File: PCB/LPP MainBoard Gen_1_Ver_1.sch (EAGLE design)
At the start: 48 parts, among them IC1 FE1.1S, U1 MAX15070, U3 IFX007T, U4 MAX15070, U5 IFX007T, U7 Pill STM32G431, U8 Blue Pill STM32F103

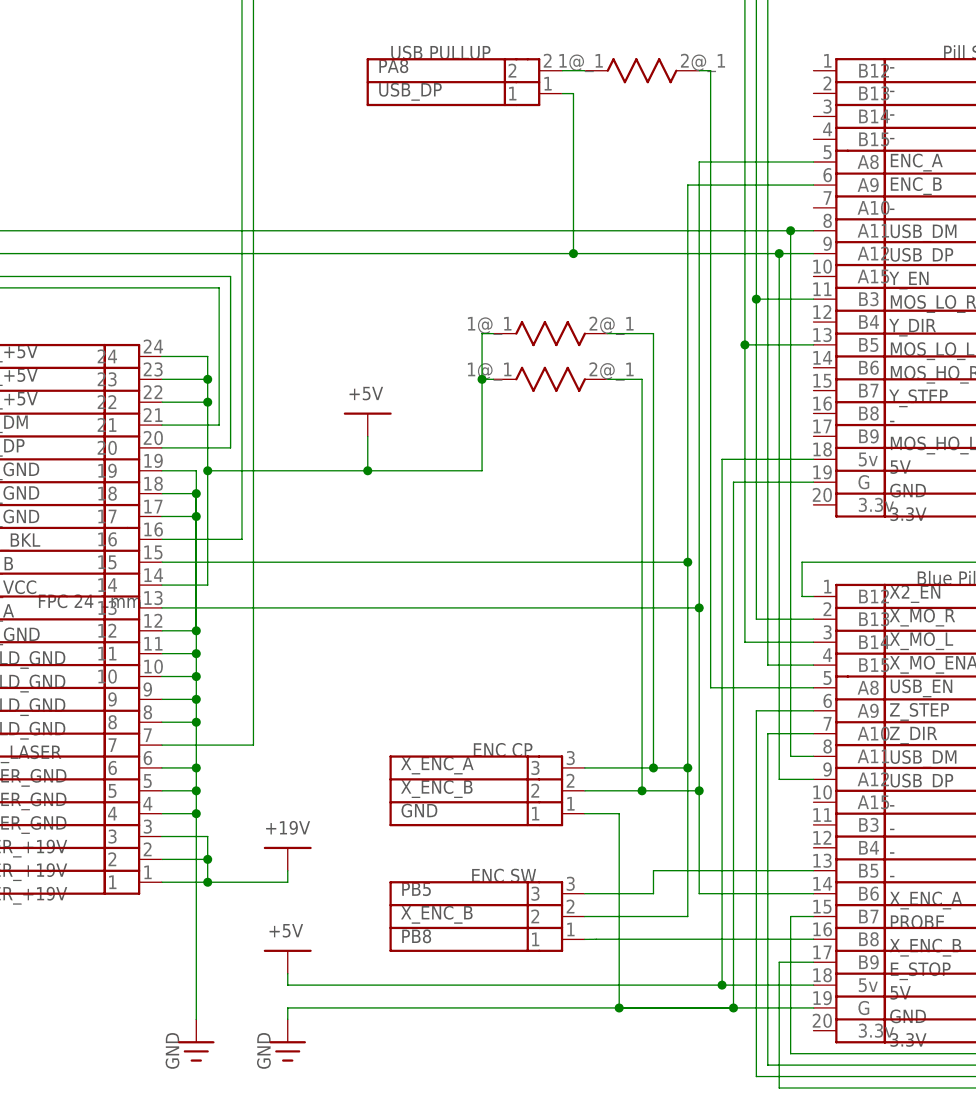
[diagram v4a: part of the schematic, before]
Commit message: modified:   PCB/LPP MainBoard Gen_1_Ver_1.brd 	modified:   PCB/LPP MainBoard Gen_1_Ver_1.sch 	modified:   PCB/LPP_MainBoard_Gen_1_Ver_1.dch 	modified:   PCB/LPP_MainBoard_Gen_1_Ver_1.dip
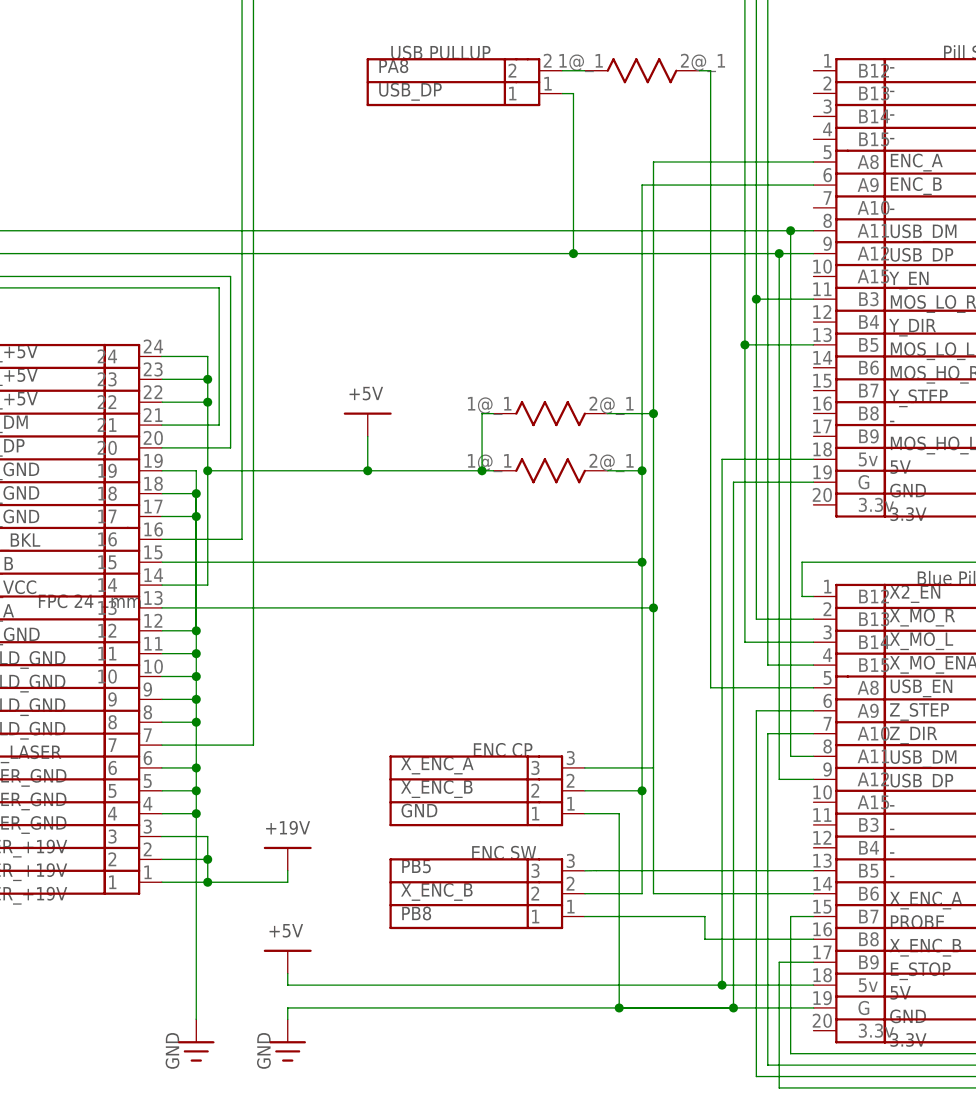
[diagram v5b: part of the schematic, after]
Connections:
- new net Сеть_33: ENC_CP.2, ENC_SW.2, FPC.15, R14.2, U7.A9
- net Сеть_10: now also FPC.13, U7.A8; no longer ENC_CP.3, ENC_SW.2, FPC.15, U7.A9
- net Сеть_6: now also ENC_CP.3; no longer ENC_CP.2, FPC.13, R14.2, U7.A8

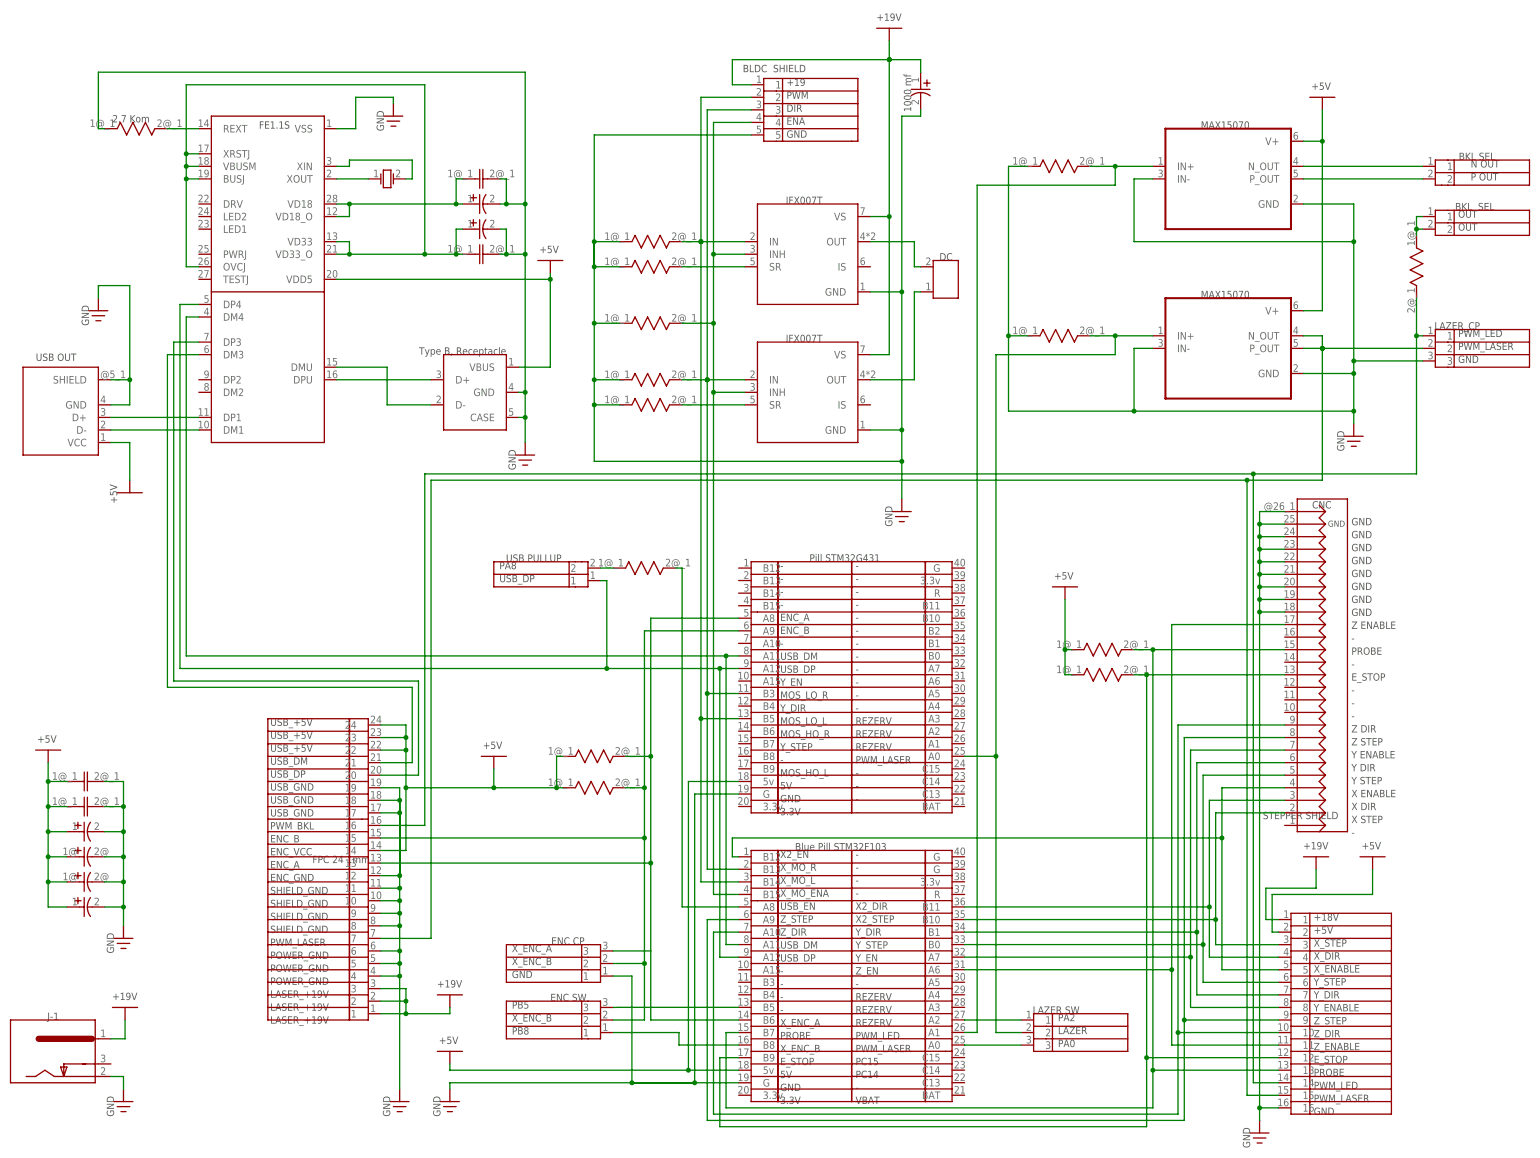
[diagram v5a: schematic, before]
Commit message: modified:   LPP_STM32F103Cx/Core/Src/main.c 	modified:   LPP_STM32F103Cx/LPP_STM32F103Cx.ioc 	modified:   LPP_STM32F103Cx/MDK-ARM/JLinkLog.txt 	modified:   LPP_STM32F103Cx/MDK-ARM/LPP_STM32F103Cx.uvguix.user 	modified:   LPP_STM32F103Cx/MDK-ARM/LPP_STM32F103Cx/LPP_STM32F103Cx.axf 	modified:   LPP_STM32F103Cx/MDK-ARM/LPP_STM32F103Cx/LPP_STM32F103Cx.build_log.htm 	modified:   LPP_STM32F103Cx/MDK-ARM/LPP_STM32F103Cx/LPP_STM32F103Cx.hex 	modified:   LPP_STM32F103Cx/MDK-ARM/LPP_STM32F103Cx/LPP_STM32F103Cx.htm 	modified:   LPP_STM32F103Cx/MDK-ARM/LPP_STM32F103Cx/LPP_STM32F103Cx.map 	modified:   LPP_STM32F103Cx/MDK-ARM/LPP_STM32F103Cx/LPP_STM32F103Cx_LPP_STM32F103Cx.dep 	modified:   LPP_STM32F103Cx/MDK-ARM/LPP_STM32F103Cx/main.o 	modified:   LPP_STM32F103Cx/MDK-ARM/counter.txt 	modified:   LPP_STM32F103Cx/My_Libraries/counter.h 	modified:   PCB/LPP MainBoard Gen_1_Ver_1.brd 	modified:   PCB/LPP MainBoard Gen_1_Ver_1.sch 	new file:   "PCB/LPP_MainBoard_Gen_1_Ver_1 \342\200\224 \320\272\320\276\320\277\320\270\321\217.dch" 	new file:   "PCB/LPP_MainBoard_Gen_1_Ver_1 \342\200\224 \320\272\320\276\320\277\320\270\321\217.dip" 	modified:   PCB/LPP_MainBoard_Gen_1_Ver_1.dch 	modified:   PCB/LPP_MainBoard_Gen_1_Ver_1.dip 	deleted:    "PCB/LPP_MainBoard_Gen_1_Ver_1/1 - \320\222\320\265\321\200\321\205\320\275\320\270\320\271.gbr" 	deleted:    "PCB/LPP_MainBoard_Gen_1_Ver_1/2 - \320\235\320\270\320\266\320\275\320\270\320\271.gbr" 	deleted:    PCB/LPP_MainBoard_Gen_1_Ver_1/Bord.lpp 	deleted:    PCB/LPP_MainBoard_Gen_1_Ver_1/Through.txt 	deleted:    PCB/LPP_MainBoard_Gen_1_Ver_1/komtur.crv3d 	deleted:    PCB/LPP_MainBoard_Gen_1_Ver_1/komtur.dxf 	deleted:    PCB/LPP_MainBoard_Gen_1_Ver_1/kontur.txt 	modified:   PCB/README.md
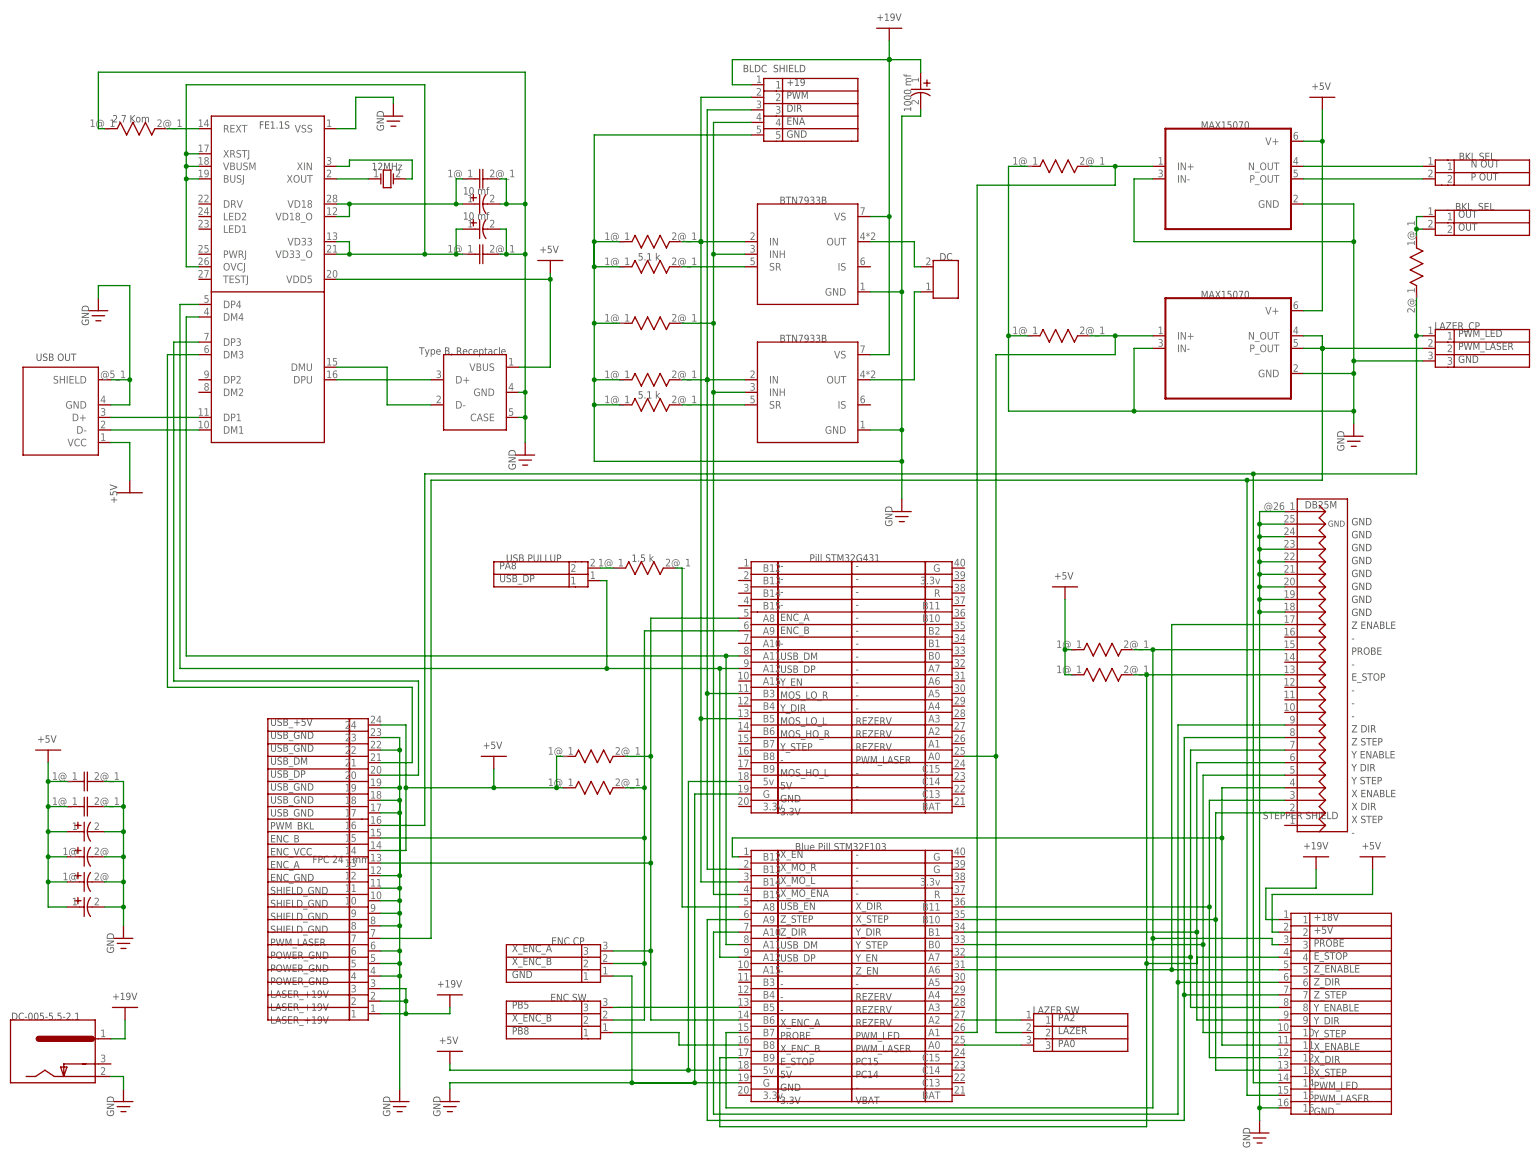
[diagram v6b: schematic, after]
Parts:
- C3, C4: value CAP_P_3MM -> 10 mf
- CNC: value CNC -> DB25M
- DC_IN: value J-1 -> DC-005-5.5-2.1
- R10: value R_0805_1206 -> 1.5 k
- R5, R9: value R_0805_1206 -> 5.1 k
- U3, U5: value IFX007T -> BTN7933B; device common:IFX007T -> common:BTN7933B
- Z: value Q_1 -> 12MHz
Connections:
- removed net Сеть_10: FPC.13, R13.2, U7.A8
- net Сеть_0: now also FPC.22, FPC.23
- net Сеть_13: now also STEPPER_SHIELD.12; no longer STEPPER_SHIELD.4
- net Сеть_17: now also STEPPER_SHIELD.4; no longer STEPPER_SHIELD.12
- net Сеть_19: now also STEPPER_SHIELD.10; no longer STEPPER_SHIELD.6
- net Сеть_20: now also STEPPER_SHIELD.9; no longer STEPPER_SHIELD.7
- net Сеть_22: now also STEPPER_SHIELD.7; no longer STEPPER_SHIELD.9
- net Сеть_25: now also STEPPER_SHIELD.6; no longer STEPPER_SHIELD.10
- net Сеть_26: now also STEPPER_SHIELD.5; no longer STEPPER_SHIELD.11
- net Сеть_29: now also STEPPER_SHIELD.11; no longer STEPPER_SHIELD.5
- net Сеть_32: now also STEPPER_SHIELD.3; no longer STEPPER_SHIELD.13
- net Сеть_36: now also STEPPER_SHIELD.13; no longer STEPPER_SHIELD.3
- net Сеть_6: now also FPC.13, R13.2, U7.A8
- net Сеть_7: no longer FPC.22, FPC.23
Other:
- note added: "+18V +5V PROBE E_STOP Z_ENABLE Z_DIR Z_STEP Y_ENABLE Y_DIR Y_STEP X_ENABLE X_DIR X_STEP PWM_LED PWM_LASER GND"
- note added: "- - - - X_DIR X_STEP Y_DIR Y_STEP Y_EN Z_EN - REZERV REZERV REZERV PWM_LED PWM_LASER PC15 PC14 - VBAT"
- note added: "1.5 k"
- note added: "10 mf"
- note added: "12MHz"
- note added: "5.1 k"
- note added: "BTN7933B"
- note added: "DB25M"
- note added: "DC-005-5.5-2.1"
- note added: "USB_+5V USB_GND USB_GND USB_DM USB_DP USB_GND USB_GND USB_GND PWM_BKL ENC_B ENC_VCC ENC_A ENC_GND SHIELD_GND SHIELD_GND SHIELD_GND SHIELD_GND PWM_LASER POWER_GND POWER_GND POWER_GND LASER_+19V LASER_+19V LASER_+19V"
- note added: "X_EN X_MO_R X_MO_L X_MO_ENA USB_EN Z_STEP Z_DIR USB_DM USB_DP - - - - X_ENC_A PROBE X_ENC_B E_STOP 5V GND 3.3V"
- note removed: "+18V +5V X_STEP X_DIR X_ENABLE Y_STEP Y_DIR Y_ENABLE Z_STEP Z_DIR Z_ENABLE E_STOP PROBE PWM_LED PWM_LASER GND"
- note removed: "- - - - X2_DIR X2_STEP Y_DIR Y_STEP Y_EN Z_EN - REZERV REZERV REZERV PWM_LED PWM_LASER PC15 PC14 - VBAT"
- note removed: "CNC"
- note removed: "IFX007T"
- note removed: "J-1"
- note removed: "USB_+5V USB_+5V USB_+5V USB_DM USB_DP USB_GND USB_GND USB_GND PWM_BKL ENC_B ENC_VCC ENC_A ENC_GND SHIELD_GND SHIELD_GND SHIELD_GND SHIELD_GND PWM_LASER POWER_GND POWER_GND POWER_GND LASER_+19V LASER_+19V LASER_+19V"
- note removed: "X2_EN X_MO_R X_MO_L X_MO_ENA USB_EN Z_STEP Z_DIR USB_DM USB_DP - - - - X_ENC_A PROBE X_ENC_B E_STOP 5V GND 3.3V"
